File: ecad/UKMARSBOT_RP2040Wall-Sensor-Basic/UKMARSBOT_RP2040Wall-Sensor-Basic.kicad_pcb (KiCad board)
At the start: 2 copper layers, 80 x 31.2 mm, 30 parts, among them J1 Conn_01x16, Q1 BC337-40, Q2 BC337-40

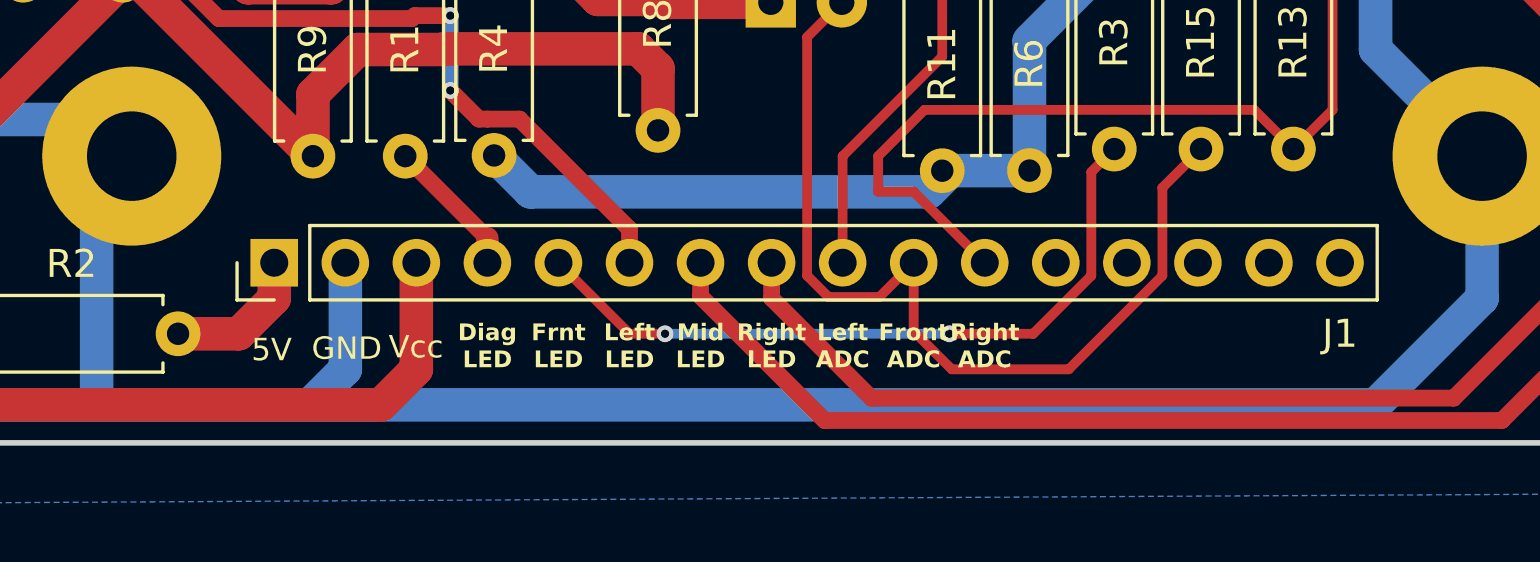
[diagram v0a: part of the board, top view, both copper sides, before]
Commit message: Update wall sensor board connector to socket and transistor base resistor values
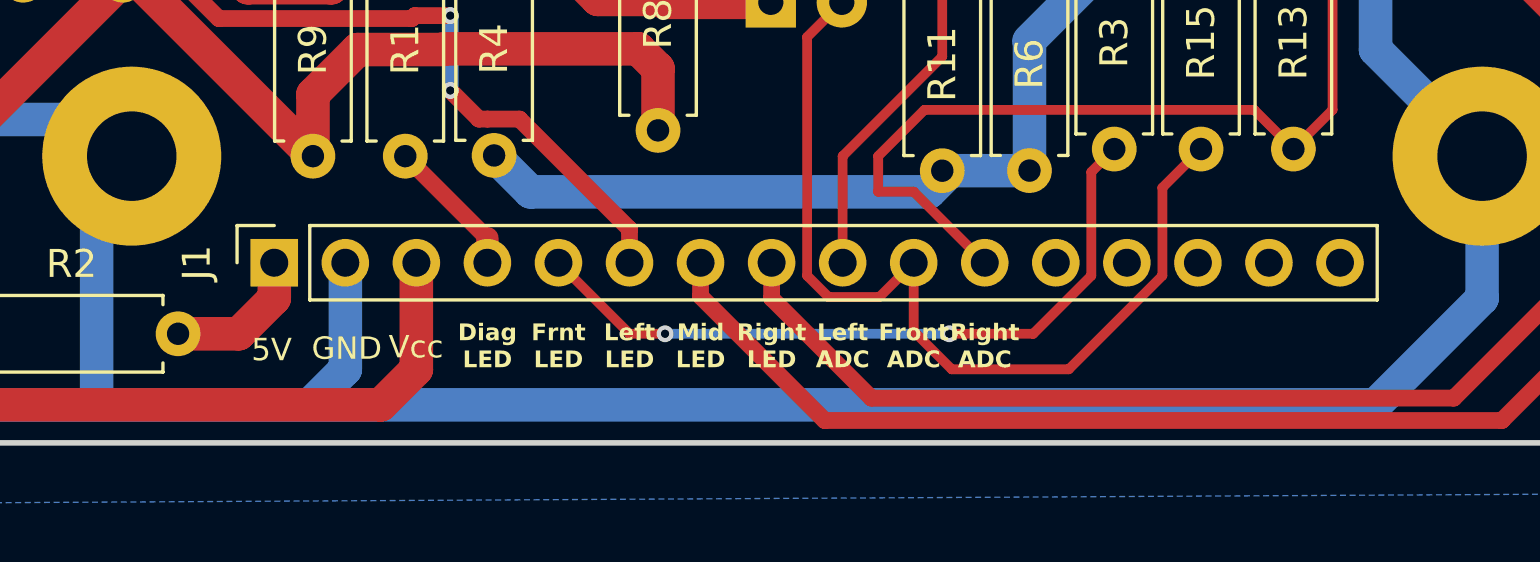
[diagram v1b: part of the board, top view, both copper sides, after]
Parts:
- J1: footprint Connector_PinHeader_2.54mm:PinHeader_1x16_P2.54mm_Vertical -> Connector_PinSocket_2.54mm:PinSocket_1x16_P2.54mm_Vertical
- R1, R3: value 220R -> 390R
- R4, R6: value 47K -> 10K
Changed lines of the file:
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@@
 		)
 	)
-	(footprint "Connector_PinHeader_2.54mm:PinHeader_1x16_P2.54mm_Vertical"
+	(footprint "Connector_PinSocket_2.54mm:PinSocket_1x16_P2.54mm_Vertical"
 		(layer "F.Cu")
 		(at 121.59 147.46 90)
-		(descr "Through hole straight pin header, 1x16, 2.54mm pitch, single row")
-		(tags "Through hole pin header THT 1x16 2.54mm single row")
+		(descr "Through hole straight socket strip, 1x16, 2.54mm pitch, single row (from Kicad 4.0.7), script generated")
+		(tags "Through hole socket strip THT 1x16 2.54mm single row")
 		(property "Reference" "J1"
-			(at -2.54 38.1 0)
+			(at 0 -2.77 90)
 			(layer "F.SilkS")
 			(effects
@@
 		)
 		(property "Value" "Conn_01x16"
-			(at 2.54 40.43 90)
+			(at 0 40.87 90)
 			(layer "F.Fab")
 			(effects
@@
 			)
 		)
-		(property "Footprint" "Connector_PinHeader_2.54mm:PinHeader_1x16_P2.54mm_Vertical"
+		(property "Footprint" "Connector_PinSocket_2.54mm:PinSocket_1x16_P2.54mm_Vertical"
 			(at 0 0 90)
 			(unlocked yes)
@@
 		(attr through_hole)
 		(fp_line
-			(start -1.33 -1.33)
-			(end 0 -1.33)
+			(start 1.33 -1.33)
+			(end 1.33 0)
 			(stroke
 				(width 0.12)
@@
 		)
 		(fp_line
-			(start -1.33 0)
-			(end -1.33 -1.33)
+			(start 0 -1.33)
+			(end 1.33 -1.33)
 			(stroke
 				(width 0.12)
@@
 		)
 		(fp_line
-			(start 1.8 -1.8)
-			(end -1.8 -1.8)
+			(start 1.75 -1.8)
+			(end 1.75 39.9)
 			(stroke
 				(width 0.05)
@@
 		(fp_line
 			(start -1.8 -1.8)
-			(end -1.8 39.9)
+			(end 1.75 -1.8)
 			(stroke
 				(width 0.05)
@@
 		)
 		(fp_line
-			(start 1.8 39.9)
-			(end 1.8 -1.8)
+			(start 1.75 39.9)
+			(end -1.8 39.9)
 			(stroke
 				(width 0.05)
@@
 		(fp_line
 			(start -1.8 39.9)
-			(end 1.8 39.9)
+			(end -1.8 -1.8)
 			(stroke
 				(width 0.05)
@@
 		)
 		(fp_line
-			(start 1.27 -1.27)
-			(end 1.27 39.37)
+			(start 0.635 -1.27)
+			(end 1.27 -0.635)
 			(stroke
 				(width 0.1)
@@
 		)
 		(fp_line
-			(start -0.635 -1.27)
-			(end 1.27 -1.27)
+			(start -1.27 -1.27)
+			(end 0.635 -1.27)
 			(stroke
 				(width 0.1)
@@
 		)
 		(fp_line
-			(start -1.27 -0.635)
-			(end -0.635 -1.27)
+			(start 1.27 -0.635)
+			(end 1.27 39.37)
 			(stroke
 				(width 0.1)
@@
 		(fp_line
 			(start -1.27 39.37)
-			(end -1.27 -0.635)
+			(end -1.27 -1.27)
 			(stroke
 				(width 0.1)
@@
 		)
 		(fp_text user "${REFERENCE}"
-			(at 0 19.05 0)
+			(at 0 19.05 180)
 			(layer "F.Fab")
 			(effects
@@
 			(pintype "passive+no_connect")
 		)
-		(model "${KICAD8_3DMODEL_DIR}/Connector_PinHeader_2.54mm.3dshapes/PinHeader_1x16_P2.54mm_Vertical.wrl"
+		(model "${KICAD8_3DMODEL_DIR}/Connector_PinSocket_2.54mm.3dshapes/PinSocket_1x16_P2.54mm_Vertical.wrl"
 			(offset
 				(xyz 0 0 0)
@@
 			)
 		)
-		(property "Value" "220R"
+		(property "Value" "390R"
 			(at 3.81 2.37 90)
 			(layer "F.Fab")
@@
 			)
 		)
-		(property "Value" "220R"
+		(property "Value" "390R"
 			(at 3.81 2.37 90)
 			(layer "F.Fab")
@@
 			)
 		)
-		(property "Value" "47K"
+		(property "Value" "10K"
 			(at 3.81 2.37 90)
 			(layer "F.Fab")
@@
 			)
 		)
-		(property "Value" "47K"
+		(property "Value" "10K"
 			(at 3.81 2.37 90)
 			(layer "F.Fab")

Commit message: V2.1 Boards ready for fabrication
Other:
- board text added: "Version 2.1"
- board text added: "v2.1 2025-08-16"
- board text removed: "Version 2.0"
- board text removed: "v2.0 2025-07-07"
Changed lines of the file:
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@@
 			(drillshape 0)
 			(scaleselection 1)
-			(outputdirectory "C:/Users/Ian/Documents/GitHub/gemini/ecad/UKMARSBOT_RP2040Wall-Sensor-Basic/fab/")
+			(outputdirectory "fab/")
 		)
 	)
@@
 		)
 	)
-	(gr_text "Version 2.0"
+	(gr_text "Version 2.1"
 		(at 176.2 152.54 0)
 		(layer "B.SilkS")
@@
 		)
 	)
-	(gr_text "v2.0 2025-07-07"
+	(gr_text "v2.1 2025-08-16"
 		(at 173.66 152.54 0)
 		(layer "F.SilkS")
